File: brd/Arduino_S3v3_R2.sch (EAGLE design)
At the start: 35 parts, among them J2 PORT C(A0-A5), J4 USB_B_PTH, U1 FT232RL, U2 ATMEGA328P_TQFP, Y1 16MHz

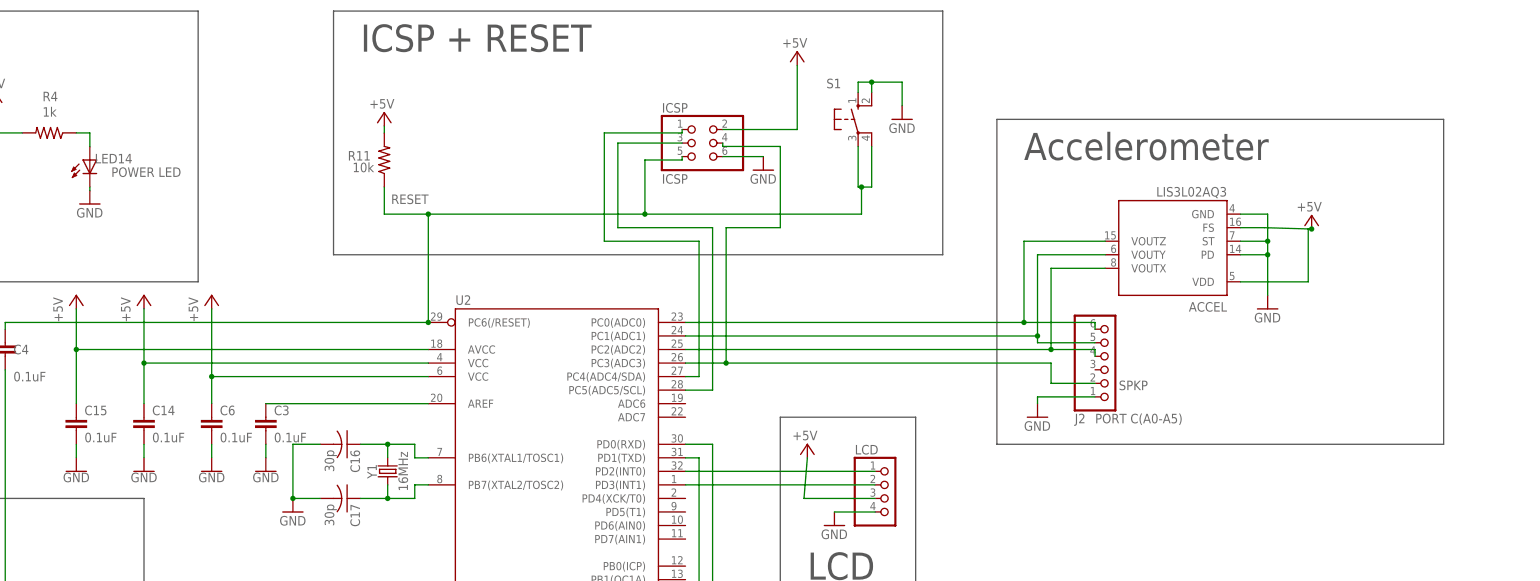
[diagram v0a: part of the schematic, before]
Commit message: Added buzzer, adjusted for SPI, new accel, pot in
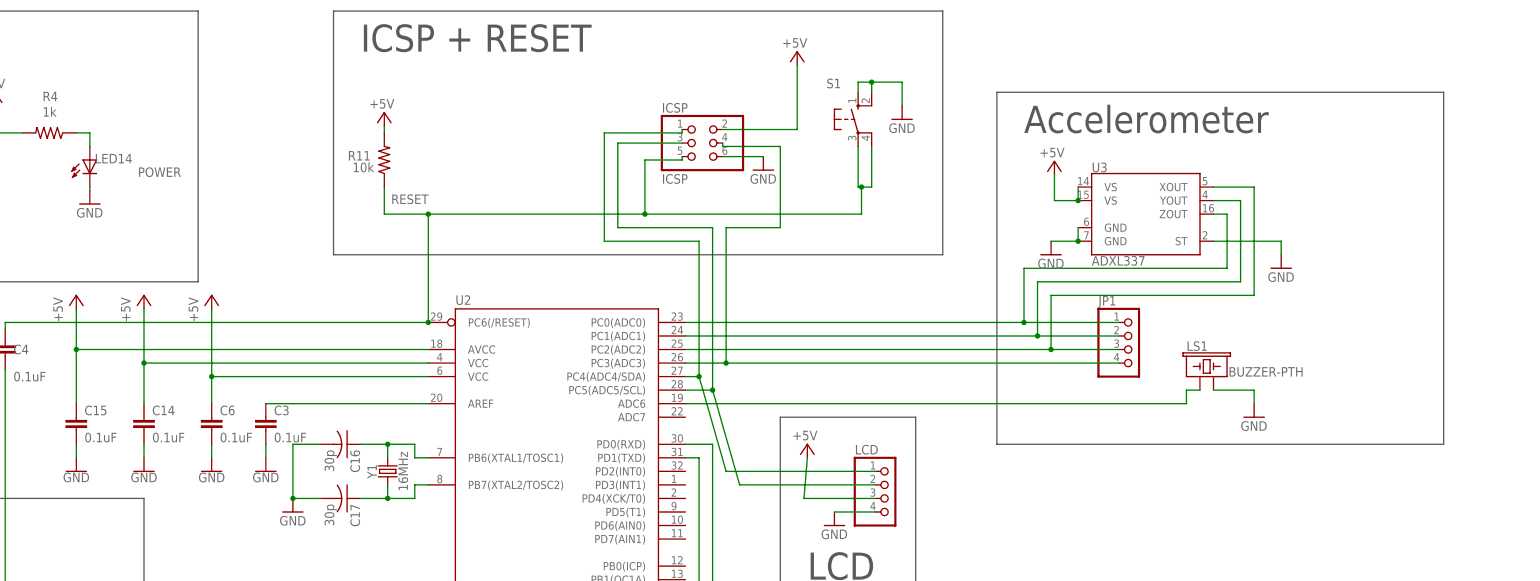
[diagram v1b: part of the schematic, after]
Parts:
- removed ACCEL: LIS3L02AQ3, st-microelectronics:LIS3L02AQ3
- removed J2: PORT C(A0-A5), pinhead:PINHD-1X6
- added JP1: (no value), pinhead:PINHD-1X4
- added LS1: BUZZER-PTH, SparkFun-Electromechanical:BUZZER-PTH
- added U3: ADXL337, SparkFun-Sensors:ADXL337
- LED14: value POWER LED -> POWER
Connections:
- net N$35 renamed RXLED
- net N$36 renamed TXLED
- net N$49 renamed RXD
- net N$50 renamed TXD
- removed net N$1: LCD.2, U2.PD3(INT1)
- removed net N$10: ACCEL.VOUTZ, J2.6, U2.PC0(ADC0)
- removed net N$11: ACCEL.VOUTY, J2.5, U2.PC1(ADC1)
- removed net N$12: ACCEL.VOUTX, J2.4, U2.PC2(ADC2)
- removed net N$51: LCD.1, U2.PD2(INT0)
- removed net SPKP: ICSP.4, J2.2, U2.PC3(ADC3)
- new net BUZZ: LS1.1, U2.ADC6
- new net POTIN: ICSP.4, JP1.4, U2.PC3(ADC3)
- new net XOUT: JP1.3, U2.PC2(ADC2), U3.XOUT
- new net YOUT: JP1.2, U2.PC1(ADC1), U3.YOUT
- new net ZOUT: JP1.1, U2.PC0(ADC0), U3.ZOUT
- net +5V: now also U3.VS@1, U3.VS@2; no longer ACCEL.FS, ACCEL.VDD
- net GND: now also LS1.2, U3.GND@1, U3.GND@2, U3.ST; no longer ACCEL.GND, ACCEL.PD, ACCEL.ST, J2.1
- net N$14: now also LCD.1
- net N$15: now also LCD.2

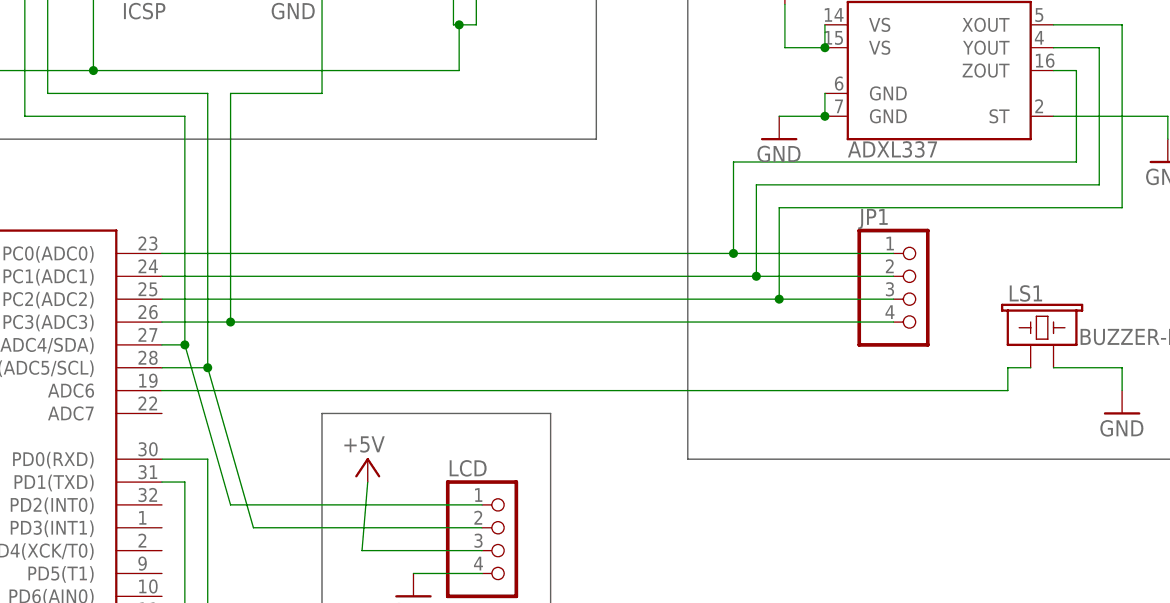
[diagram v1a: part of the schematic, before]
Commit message: Board design final dimensions. Rough Draft ready.
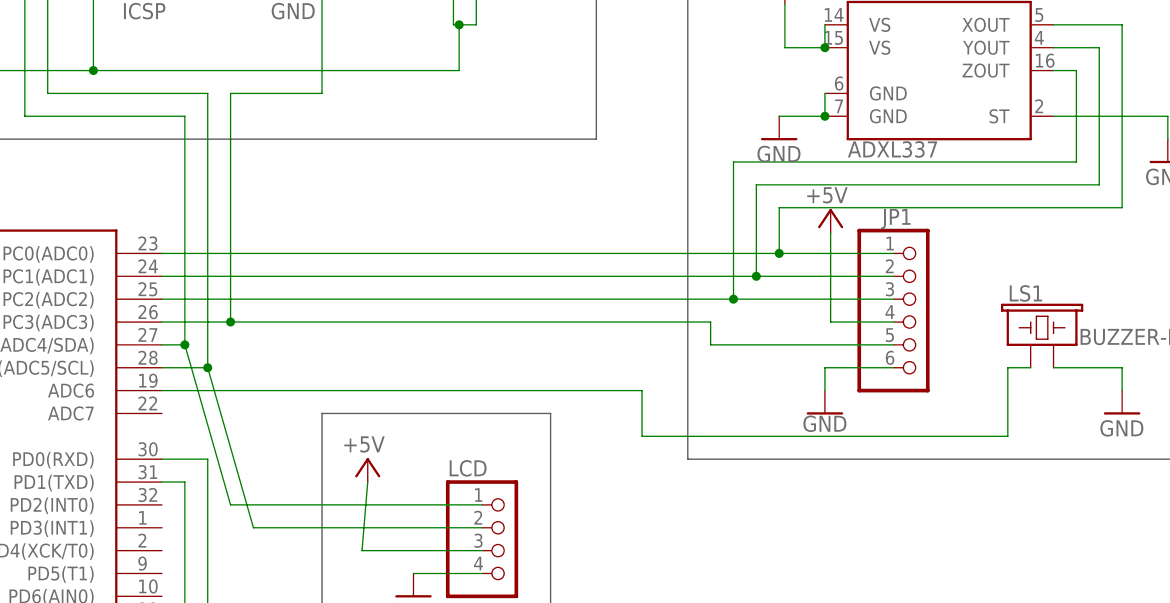
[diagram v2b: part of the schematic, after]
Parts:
- JP1: device pinhead:PINHD-1X4 -> adafruit:PINHD-1X6
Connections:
- net +5V: now also JP1.4
- net GND: now also JP1.6
- net POTIN: now also JP1.5; no longer JP1.4
- net XOUT: now also U3.ZOUT; no longer U3.XOUT
- net ZOUT: now also U3.XOUT; no longer U3.ZOUT
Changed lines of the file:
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@@
 <part name="GND3" library="supply1" library_urn="urn:adsk.eagle:library:371" deviceset="GND" device=""/>
 <part name="GND27" library="supply1" library_urn="urn:adsk.eagle:library:371" deviceset="GND" device=""/>
-<part name="JP1" library="pinhead" library_urn="urn:adsk.eagle:library:325" deviceset="PINHD-1X4" device="" package3d_urn="urn:adsk.eagle:package:22407/2"/>
+<part name="JP1" library="adafruit" library_urn="urn:adsk.eagle:library:420" deviceset="PINHD-1X6" device="" package3d_urn="urn:adsk.eagle:package:6240711/1"/>
 <part name="LS1" library="SparkFun-Electromechanical" library_urn="urn:adsk.eagle:library:516" deviceset="BUZZER" device="-PTH" package3d_urn="urn:adsk.eagle:package:38558/1"/>
 <part name="U3" library="SparkFun-Sensors" library_urn="urn:adsk.eagle:library:534" deviceset="ADXL337" device="" package3d_urn="urn:adsk.eagle:package:39959/1"/>
 <part name="GND8" library="supply1" deviceset="GND" device=""/>
+<part name="GND28" library="SparkFun-PowerSymbols" library_urn="urn:adsk.eagle:library:530" deviceset="GND" device=""/>
+<part name="P+8" library="supply1" deviceset="+5V" device=""/>
 </parts>
 <sheets>
@@
 <attribute name="VALUE" x="327.66" y="93.98" size="1.778" layer="96"/>
 </instance>
-<instance part="JP1" gate="A" x="307.34" y="109.22" smashed="yes">
-<attribute name="NAME" x="300.99" y="117.475" size="1.778" layer="95"/>
-<attribute name="VALUE" x="300.99" y="101.6" size="1.778" layer="96"/>
+<instance part="JP1" gate="A" x="307.34" y="106.68" smashed="yes">
+<attribute name="NAME" x="303.53" y="117.475" size="1.778" layer="95"/>
+<attribute name="VALUE" x="300.99" y="99.06" size="1.778" layer="96"/>
 </instance>
 <instance part="LS1" gate="G$1" x="320.04" y="104.14" smashed="yes">
@@
 <instance part="GND8" gate="1" x="335.28" y="124.46" smashed="yes">
 <attribute name="VALUE" x="332.74" y="121.92" size="1.778" layer="96"/>
+</instance>
+<instance part="GND28" gate="1" x="297.18" y="96.52" smashed="yes">
+<attribute name="VALUE" x="297.18" y="96.266" size="1.778" layer="96" align="top-center"/>
+</instance>
+<instance part="P+8" gate="1" x="297.815" y="119.126" smashed="yes">
+<attribute name="VALUE" x="299.72" y="121.666" size="1.778" layer="96" rot="R180"/>
 </instance>
 </instances>
@@
 <wire x1="297.18" y1="139.7" x2="297.18" y2="137.16" width="0.1524" layer="91"/>
 <junction x="297.18" y="137.16"/>
+</segment>
+<segment>
+<pinref part="P+8" gate="1" pin="+5V"/>
+<pinref part="JP1" gate="A" pin="4"/>
+<wire x1="297.815" y1="116.586" x2="297.815" y2="106.68" width="0.1524" layer="91"/>
+<wire x1="297.815" y1="106.68" x2="304.8" y2="106.68" width="0.1524" layer="91"/>
 </segment>
 </net>
@@
 <pinref part="GND8" gate="1" pin="GND"/>
 <wire x1="335.28" y1="129.54" x2="335.28" y2="127" width="0.1524" layer="91"/>
+</segment>
+<segment>
+<pinref part="GND28" gate="1" pin="GND"/>
+<pinref part="JP1" gate="A" pin="6"/>
+<wire x1="297.18" y1="99.06" x2="297.18" y2="101.6" width="0.1524" layer="91"/>
+<wire x1="297.18" y1="101.6" x2="304.8" y2="101.6" width="0.1524" layer="91"/>
 </segment>
 </net>
@@
 <segment>
 <pinref part="U2" gate="U$1" pin="PC0(ADC0)"/>
-<wire x1="223.52" y1="114.3" x2="287.02" y2="114.3" width="0.1524" layer="91"/>
-<wire x1="287.02" y1="124.46" x2="287.02" y2="114.3" width="0.1524" layer="91"/>
+<wire x1="223.52" y1="114.3" x2="292.1" y2="114.3" width="0.1524" layer="91"/>
 <pinref part="JP1" gate="A" pin="1"/>
-<wire x1="287.02" y1="114.3" x2="304.8" y2="114.3" width="0.1524" layer="91"/>
-<junction x="287.02" y="114.3"/>
-<wire x1="287.02" y1="124.46" x2="325.12" y2="124.46" width="0.1524" layer="91"/>
-<wire x1="325.12" y1="124.46" x2="325.12" y2="134.62" width="0.1524" layer="91"/>
-<pinref part="U3" gate="G$1" pin="ZOUT"/>
-<wire x1="325.12" y1="134.62" x2="322.58" y2="134.62" width="0.1524" layer="91"/>
+<pinref part="U3" gate="G$1" pin="XOUT"/>
+<wire x1="292.1" y1="114.3" x2="304.8" y2="114.3" width="0.1524" layer="91"/>
+<wire x1="330.2" y1="139.7" x2="322.58" y2="139.7" width="0.1524" layer="91"/>
+<wire x1="330.2" y1="119.38" x2="330.2" y2="139.7" width="0.1524" layer="91"/>
+<wire x1="292.1" y1="119.38" x2="330.2" y2="119.38" width="0.1524" layer="91"/>
+<wire x1="292.1" y1="119.38" x2="292.1" y2="114.3" width="0.1524" layer="91"/>
+<junction x="292.1" y="114.3"/>
 </segment>
 </net>
@@
 <segment>
 <pinref part="U2" gate="U$1" pin="PC1(ADC1)"/>
-<wire x1="289.56" y1="121.92" x2="289.56" y2="111.76" width="0.1524" layer="91"/>
+<wire x1="304.8" y1="111.76" x2="289.56" y2="111.76" width="0.1524" layer="91"/>
+<pinref part="JP1" gate="A" pin="2"/>
+<pinref part="U3" gate="G$1" pin="YOUT"/>
 <wire x1="289.56" y1="111.76" x2="223.52" y2="111.76" width="0.1524" layer="91"/>
-<pinref part="JP1" gate="A" pin="2"/>
-<wire x1="289.56" y1="111.76" x2="304.8" y2="111.76" width="0.1524" layer="91"/>
-<junction x="289.56" y="111.76"/>
-<wire x1="289.56" y1="121.92" x2="327.66" y2="121.92" width="0.1524" layer="91"/>
-<pinref part="U3" gate="G$1" pin="YOUT"/>
 <wire x1="327.66" y1="137.16" x2="322.58" y2="137.16" width="0.1524" layer="91"/>
 <wire x1="327.66" y1="121.92" x2="327.66" y2="137.16" width="0.1524" layer="91"/>
+<wire x1="289.56" y1="121.92" x2="327.66" y2="121.92" width="0.1524" layer="91"/>
+<wire x1="289.56" y1="121.92" x2="289.56" y2="111.76" width="0.1524" layer="91"/>
+<junction x="289.56" y="111.76"/>
 </segment>
 </net>
@@
 <segment>
 <pinref part="U2" gate="U$1" pin="PC2(ADC2)"/>
-<wire x1="223.52" y1="109.22" x2="292.1" y2="109.22" width="0.1524" layer="91"/>
-<wire x1="292.1" y1="119.38" x2="292.1" y2="109.22" width="0.1524" layer="91"/>
+<wire x1="223.52" y1="109.22" x2="287.02" y2="109.22" width="0.1524" layer="91"/>
 <pinref part="JP1" gate="A" pin="3"/>
-<wire x1="292.1" y1="109.22" x2="304.8" y2="109.22" width="0.1524" layer="91"/>
-<junction x="292.1" y="109.22"/>
-<wire x1="292.1" y1="119.38" x2="330.2" y2="119.38" width="0.1524" layer="91"/>
-<wire x1="330.2" y1="119.38" x2="330.2" y2="139.7" width="0.1524" layer="91"/>
-<pinref part="U3" gate="G$1" pin="XOUT"/>
-<wire x1="330.2" y1="139.7" x2="322.58" y2="139.7" width="0.1524" layer="91"/>
+<pinref part="U3" gate="G$1" pin="ZOUT"/>
+<wire x1="287.02" y1="109.22" x2="304.8" y2="109.22" width="0.1524" layer="91"/>
+<wire x1="325.12" y1="134.62" x2="322.58" y2="134.62" width="0.1524" layer="91"/>
+<wire x1="325.12" y1="124.46" x2="325.12" y2="134.62" width="0.1524" layer="91"/>
+<wire x1="287.02" y1="124.46" x2="325.12" y2="124.46" width="0.1524" layer="91"/>
+<wire x1="287.02" y1="124.46" x2="287.02" y2="109.22" width="0.1524" layer="91"/>
+<junction x="287.02" y="109.22"/>
 </segment>
 </net>
@@
 <wire x1="231.14" y1="132.08" x2="231.14" y2="106.68" width="0.1524" layer="91"/>
 <wire x1="231.14" y1="106.68" x2="223.52" y2="106.68" width="0.1524" layer="91"/>
-<wire x1="231.14" y1="106.68" x2="304.8" y2="106.68" width="0.1524" layer="91"/>
+<wire x1="231.14" y1="106.68" x2="284.48" y2="106.68" width="0.1524" layer="91"/>
+<wire x1="284.48" y1="106.68" x2="284.48" y2="104.14" width="0.1524" layer="91"/>
 <junction x="231.14" y="106.68"/>
-<pinref part="JP1" gate="A" pin="4"/>
+<pinref part="JP1" gate="A" pin="5"/>
+<wire x1="284.48" y1="104.14" x2="304.8" y2="104.14" width="0.1524" layer="91"/>
 </segment>
 </net>
@@
 <net name="BUZZ" class="0">
 <segment>
-<pinref part="U2" gate="U$1" pin="ADC6"/>
-<wire x1="223.52" y1="99.06" x2="317.5" y2="99.06" width="0.1524" layer="91"/>
-<wire x1="317.5" y1="99.06" x2="317.5" y2="101.6" width="0.1524" layer="91"/>
 <pinref part="LS1" gate="G$1" pin="1"/>
 <wire x1="317.5" y1="101.6" x2="320.04" y2="101.6" width="0.1524" layer="91"/>
-</segment>
-</net>
+<pinref part="U2" gate="U$1" pin="ADC6"/>
+<wire x1="223.52" y1="99.06" x2="276.86" y2="99.06" width="0.1524" layer="91"/>
+<wire x1="276.86" y1="99.06" x2="276.86" y2="93.98" width="0.1524" layer="91"/>
+<wire x1="276.86" y1="93.98" x2="317.5" y2="93.98" width="0.1524" layer="91"/>
+<wire x1="317.5" y1="93.98" x2="317.5" y2="101.6" width="0.1524" layer="91"/>
+</segment>
+</net>

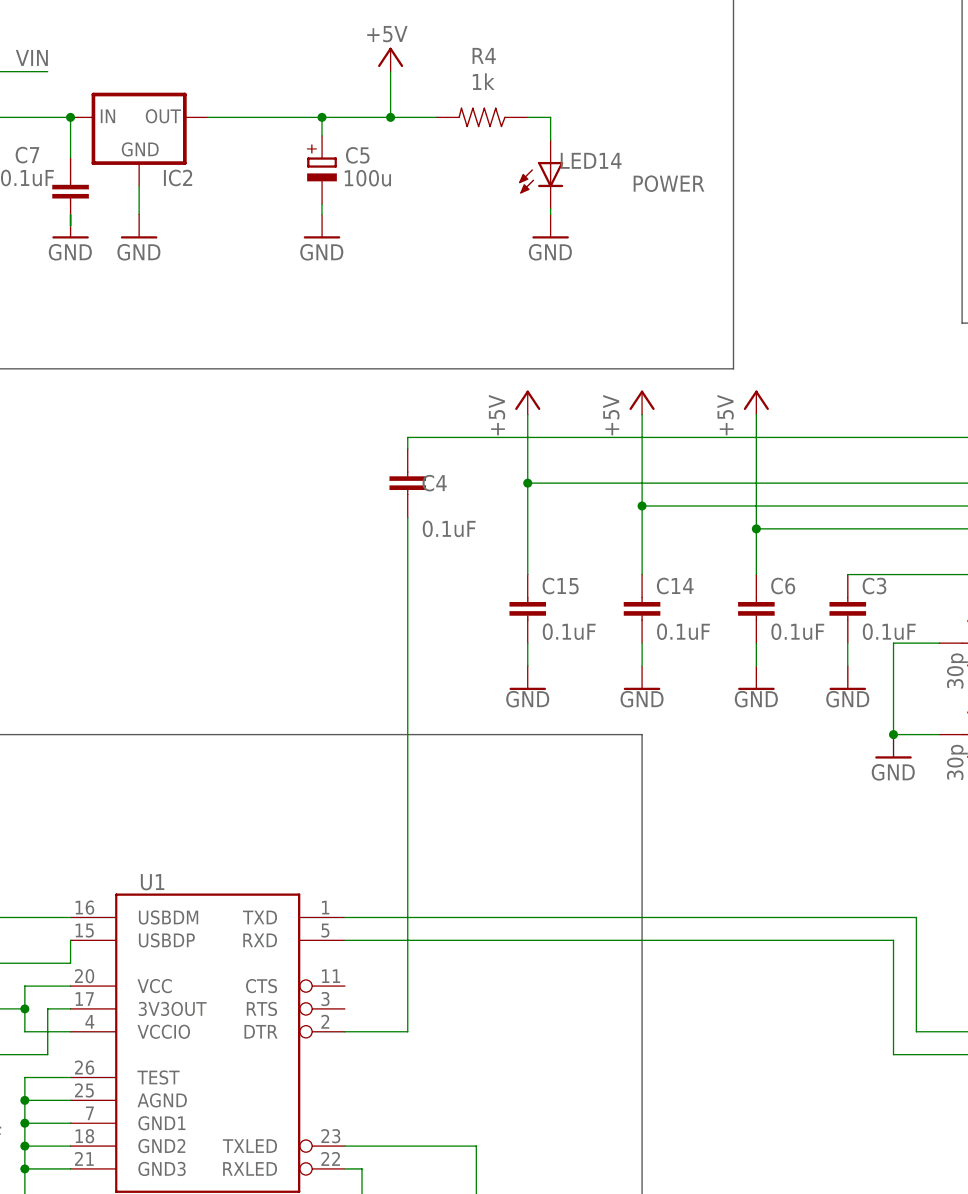
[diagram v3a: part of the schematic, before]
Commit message: Added initial manufacturing part numbers
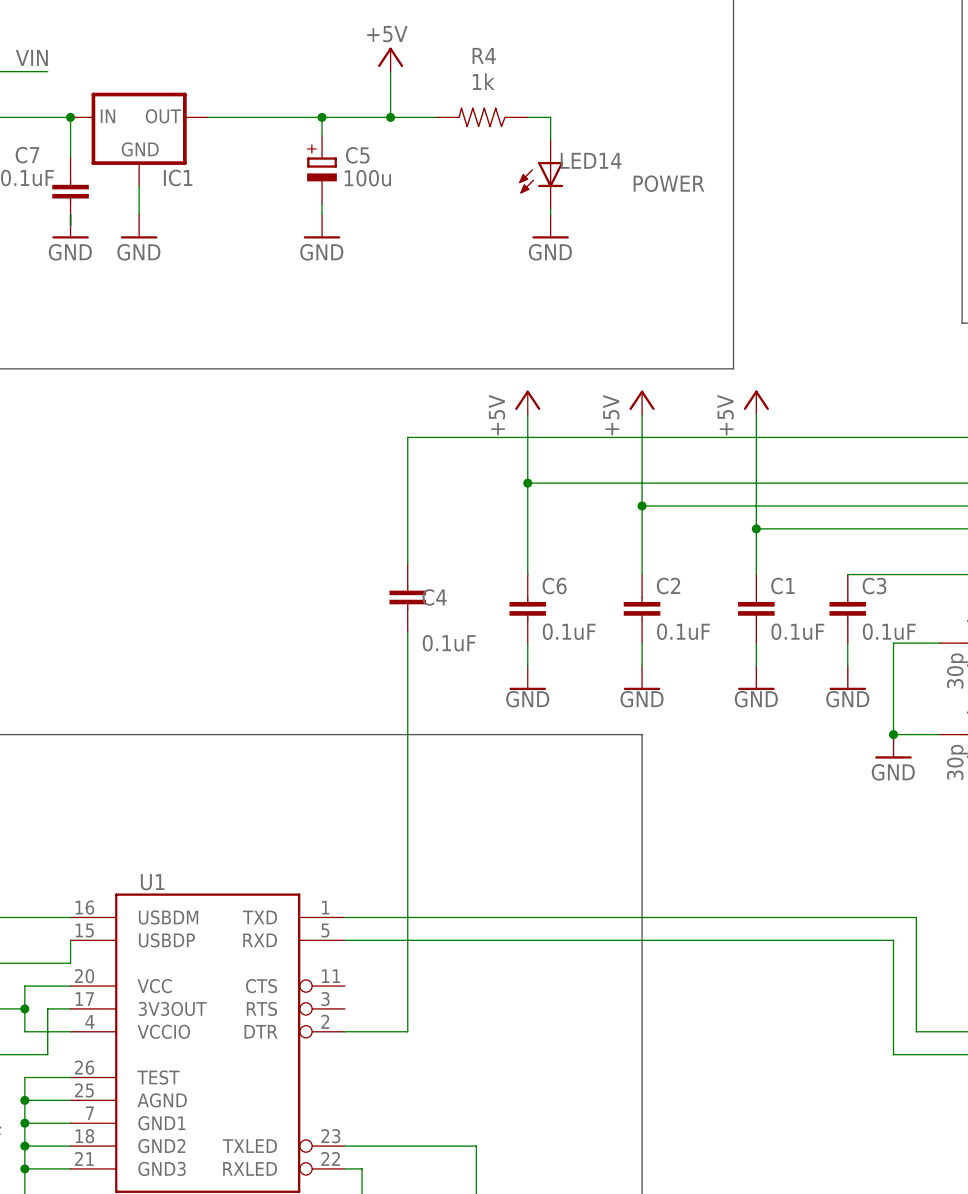
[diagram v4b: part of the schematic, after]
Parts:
- removed C15: 0.1uF, SparkFun-Capacitors:0.1UF-0603-25V-(+80/-20%)
- removed IC2: (no value), v-reg:78XXL
- added C1: 0.1uF, SparkFun-Capacitors:0.1UF-0603-25V-(+80/-20%)
- added IC1: (no value), v-reg:78XXS
- C10: MFR (none) -> KEMET; MPN (none) -> C0603C103K5RAC7013
- C11, C12, C2, C3, C4, C6, C7, C9: MFR (none) -> KEMET; MPN (none) -> C0603X104K5RAC3316
- C13: MFR (none) -> Taiyo Yuden; MPN (none) -> LMK107BJ475MAHT
- C16, C17: MFR (none) -> KEMET; MPN (none) -> C0603C300M5HACAUTO
- C5, C8: MFR (none) -> KEMET; MPN (none) -> A750BK107M1AAAE024
- D1: MFR (none) -> Diodes Incorporated; MPN (none) -> 1N4004-T
- DC1: MFR (none) -> Gravitech; MPN (none) -> CON-SOCJ-2155
- J4: MFR (none) -> Amphenol FCI; MPN (none) -> 61729-0010BLF
- L2: MFR (none) -> Murata Electronics; MPN (none) -> LQW18AS33NJ0CD
- LED14: MFR (none) -> VCC; MPN (none) -> LTH3MM12VFR4100
- LS1: MFR (none) -> TDK; MPN (none) -> SD1209T5-A1
- R1, R2, R4: MFR (none) -> Vishay / Dale; MPN (none) -> RCC06031K00FKEA
- R11: MFR (none) -> Panasonic; MPN (none) -> ERJ-UP3D1002V
- RXLED, TXLED: MFR (none) -> VCC; MPN (none) -> LTH3MM12VFR4500
- S1: MFR (none) -> Omron Electronics; MPN (none) -> B3F-1000
- U1: MFR (none) -> FTDI; MPN (none) -> FT232RL-REEL
- U2: MFR (none) -> Microchip Technology / Atmel; MPN (none) -> ATMEGA328P-AU
- renumbered C14 to C2
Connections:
- net +5V: now also C1.1, IC1.OUT; no longer C15.1, IC2.OUT
- net GND: now also C1.2, IC1.GND; no longer C15.2, IC2.GND
- net VIN: now also IC1.IN; no longer IC2.IN
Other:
- moved on the sheet: C4, C6
